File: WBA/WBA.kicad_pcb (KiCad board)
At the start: 4 copper layers, 167.4 x 89 mm, 142 parts, among them J1 Signal input, J10 Conn_01x02, J11 Conn_01x02, J12 Conn_01x02, J13 Conn_01x02, J14 Conn_01x02, J15 Conn_01x02, J16 LPF_potentiometer_100k, J17 Amp Selector, J19 Detector Input, J2 Conn_01x24, J3 Conn_01x04, J4 Conn_01x24, J5 Input Power, J6 Conn_01x04, J7 Conn_01x04, J8 Conn_01x02, J9 Conn_01x02, Q1 A03400A, Q2 A03401A, U11 MAX7424EUA+T, U12 TL072, U14 L7805, U15 L7905, U16 TPS5430DDA, U19 TLV2374IDR, U2 TLV2372, U20 TLV2374IDR, U21 OP07BRZ, U22 OP07BRZ, U23 INA128, U24 INA128, U3 MAX7424EUA+T, U8 L7805

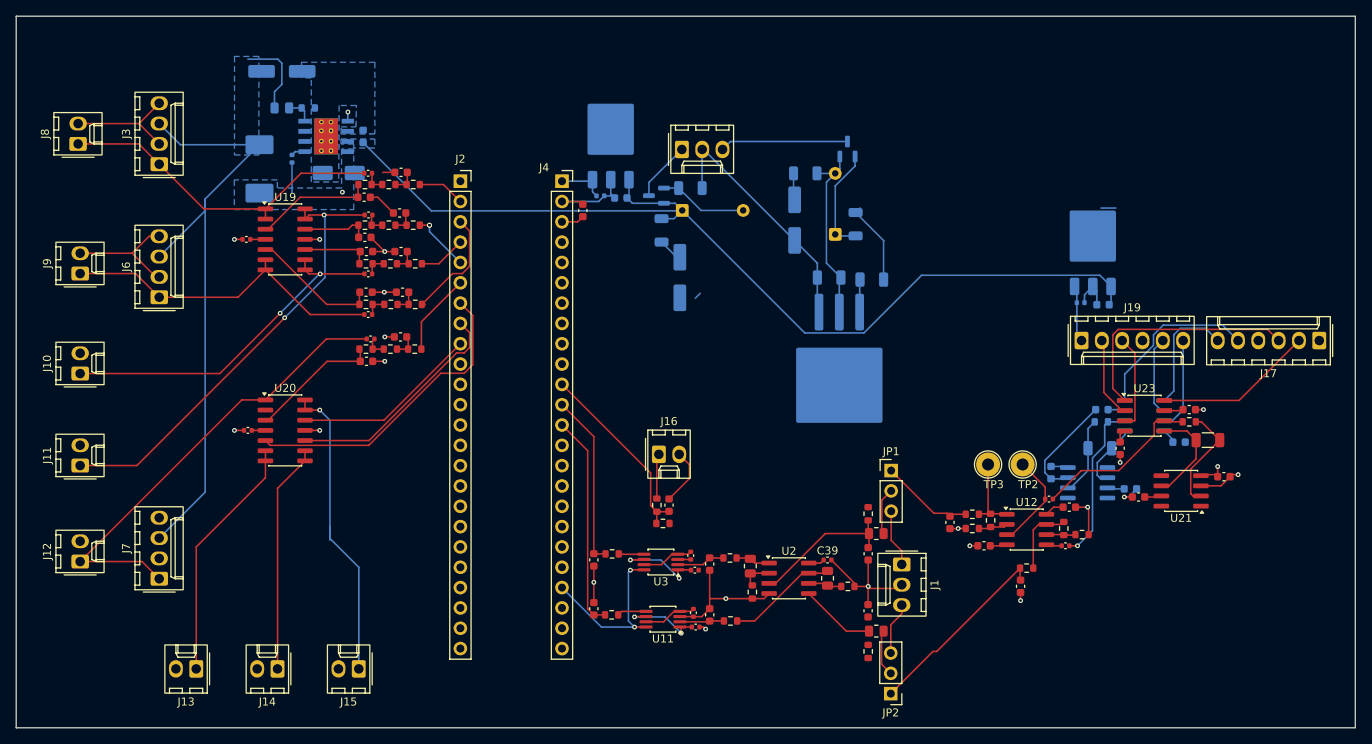
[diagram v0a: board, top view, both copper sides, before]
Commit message: more compact layout
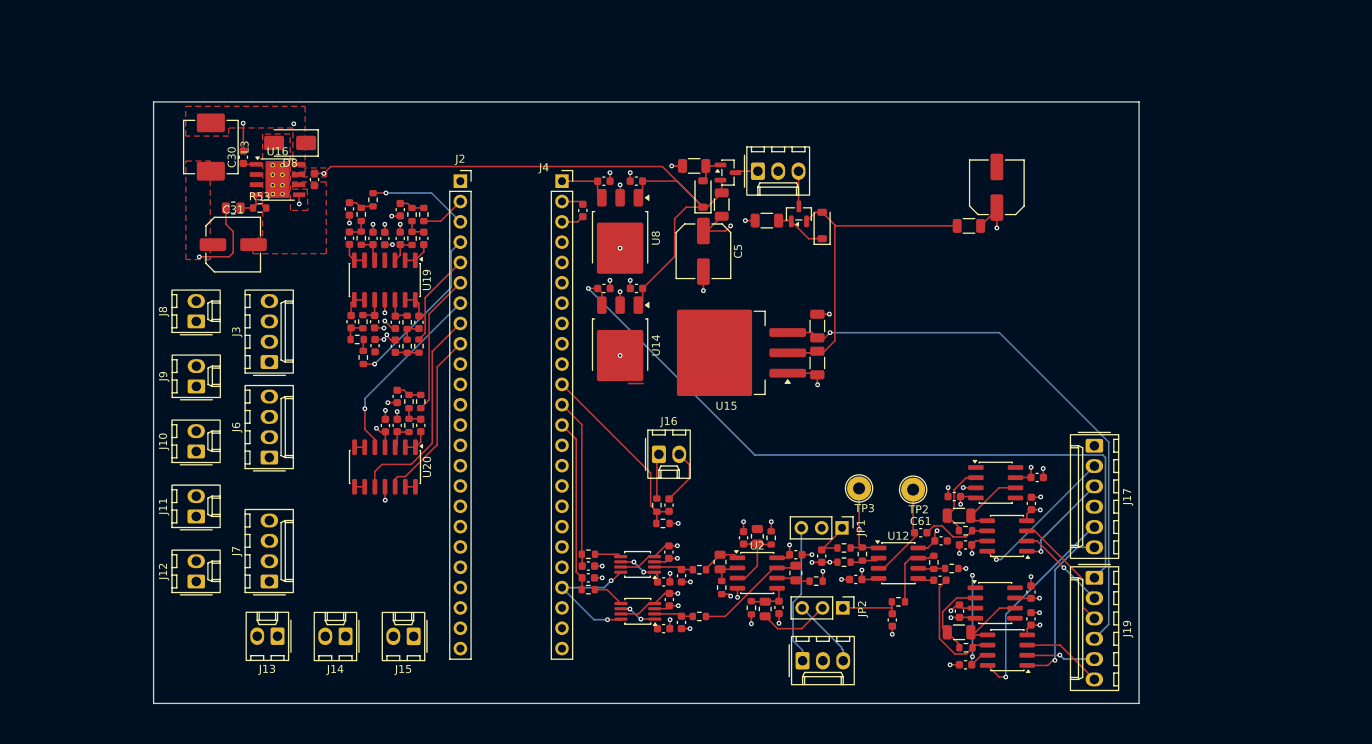
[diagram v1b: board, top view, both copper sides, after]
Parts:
- removed D3, D7: 1N4148, Diode_THT:D_DO-35_SOD27_P7.62mm_Horizontal
- added D1: 1N4148W, Diode_SMD:D_SOD-123, F.Cu at (166.0, 41.2)
- added D2: 1N4148W, Diode_SMD:D_SOD-123, F.Cu at (180.9, 45.2)
- C10, C13, C16, C19, C39, C40, C41, C42, C43, C46, C47, C61, C62, C9: footprint Capacitor_SMD:C_0402_1005Metric -> Capacitor_SMD:C_0603_1608Metric
- C28, C31, C5, C54, C6, C66, C67, C68, C71, C72, C73, C82, C83, D8, L3, Q1, Q2, R36, R38, R40, R50, R51, R52, R53, U14, U15, U16, U22, U24, U8: moved to F.Cu
- C29, C30, C81: footprint Capacitor_SMD:C_0402_1005Metric -> Capacitor_SMD:C_0603_1608Metric; moved to F.Cu
- moved U14 60.4 mm to (155.6, 60.2), turned to -90 degrees
- moved C81 59.6 mm to (153.6, 53.0)
- moved C54 58.4 mm to (157.6, 53.0)
- moved C72 36.2 mm to (198.8, 100.1)
- moved U24 34.0 mm to (204.0, 98.2)
- moved C64 33.8 mm to (197.4, 79.0), turned to 180 degrees
- moved R50 32.9 mm to (198.8, 97.9)
- moved C70 32.7 mm to (198.8, 85.1), turned to 180 degrees
- moved C65 32.5 mm to (198.0, 81.4), turned to 180 degrees
- moved R49 31.1 mm to (198.8, 83.3), turned to 0 degrees
- moved J17 31.0 mm to (214.9, 72.7), turned to -90 degrees
- moved J19 29.7 mm to (214.9, 89.2), turned to -90 degrees
- moved C68 29.0 mm to (198.0, 96.0)
- moved C71 28.8 mm to (207.0, 94.3), turned to 90 degrees
- moved J3 28.3 mm to (111.8, 62.2)
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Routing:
- net GND: track 192.4 -> 85.0 mm, vias 20 -> 57
- net +5V_{detector}: track 7.21 -> 92.5 mm, vias 0 -> 1
- net +5V_{display}: track 88.0 -> 10.4 mm
- net -5V_{detector}: track 5.94 -> 73.5 mm, vias 0 -> 1
- net Net-(J12-Pin_1): track 58.1 -> 3.49 mm
- net Net-(J11-Pin_1): track 57.1 -> 3.49 mm, vias 2 -> 0
- net Net-(J10-Pin_1): track 44.0 -> 3.39 mm, vias 2 -> 0
- net Net-(J3-Pin_1): track 42.3 -> 3.67 mm
- net Net-(D1-K): track 123.4 -> 84.9 mm, vias 1 -> 2
- net Net-(J6-Pin_1): track 41.8 -> 3.51 mm
- net Net-(J15-Pin_1): track 39.2 -> 1.27 mm, vias 1 -> 0
- net Net-(J13-Pin_1): track 30.9 -> 1.27 mm
- net Net-(J14-Pin_1): track 28.7 -> 1.27 mm
- net +15V: track 15.4 -> 33.8 mm, vias 0 -> 7
- net Net-(D2-A): track 23.3 -> 41.0 mm
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- added copper zone on In2.Cu, net +15V
- added copper zone on In2.Cu, net +3.3V
- added copper zone on F.Cu, net +5V_{display}
- added copper zone on In2.Cu, net -15V
- added copper zone on F.Cu, net GND
- added copper zone on F.Cu, net Net-(D1-K)
- added copper zone on F.Cu, net Net-(D8-K)
- removed copper zone on B.Cu, net +5V_{display}
- removed copper zone on B.Cu, net GND
- removed copper zone on B.Cu, net Net-(D1-K)
- removed copper zone on B.Cu, net Net-(D8-K)
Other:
- board size 167.4 x 89 mm -> 123.2 x 75.2 mm
